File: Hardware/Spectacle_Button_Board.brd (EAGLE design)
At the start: 44.5 x 73.7 mm, 46 parts, among them J17 AUDIO-JACK3, J19 FTDI_DEVICE, J20 AUDIO-JACK3, U1 CY8C4146LQI-S422, U2 3.3V/150mA

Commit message: first draft routing
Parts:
- moved C5 40.0 mm to (20.6, 25.0), turned to 180 degrees
- moved R2 37.7 mm to (29.5, 25.0)
- moved C6 37.7 mm to (20.8, 26.8), turned to 180 degrees
- moved D3 36.7 mm to (22.1, 29.6)
- moved C4 33.7 mm to (27.4, 42.0), turned to 90 degrees
- moved C2 33.0 mm to (24.4, 42.0)
- moved D2 33.0 mm to (28.1, 50.2)
- moved D4 33.0 mm to (15.2, 48.3)
- moved D5 33.0 mm to (15.2, 52.1)
- moved D6 33.0 mm to (15.2, 44.5)
- moved D7 33.0 mm to (15.2, 36.8)
- moved D8 33.0 mm to (15.2, 40.6)
- moved D9 33.0 mm to (15.2, 33.0)
- moved J1 33.0 mm to (27.2, 57.0)
- moved J10 33.0 mm to (36.8, 68.6)
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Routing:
- net GND: track 37.4 -> 12.6 mm, vias 0 -> 2
- net N$3: track 10.2 -> 1.40 mm
- net VIN: track 51.7 -> 46.6 mm
- net N$5: track 8.66 -> 4.85 mm
- net 3.3V: track 79.1 -> 75.3 mm
- net SCL: track 44.3 -> 46.2 mm

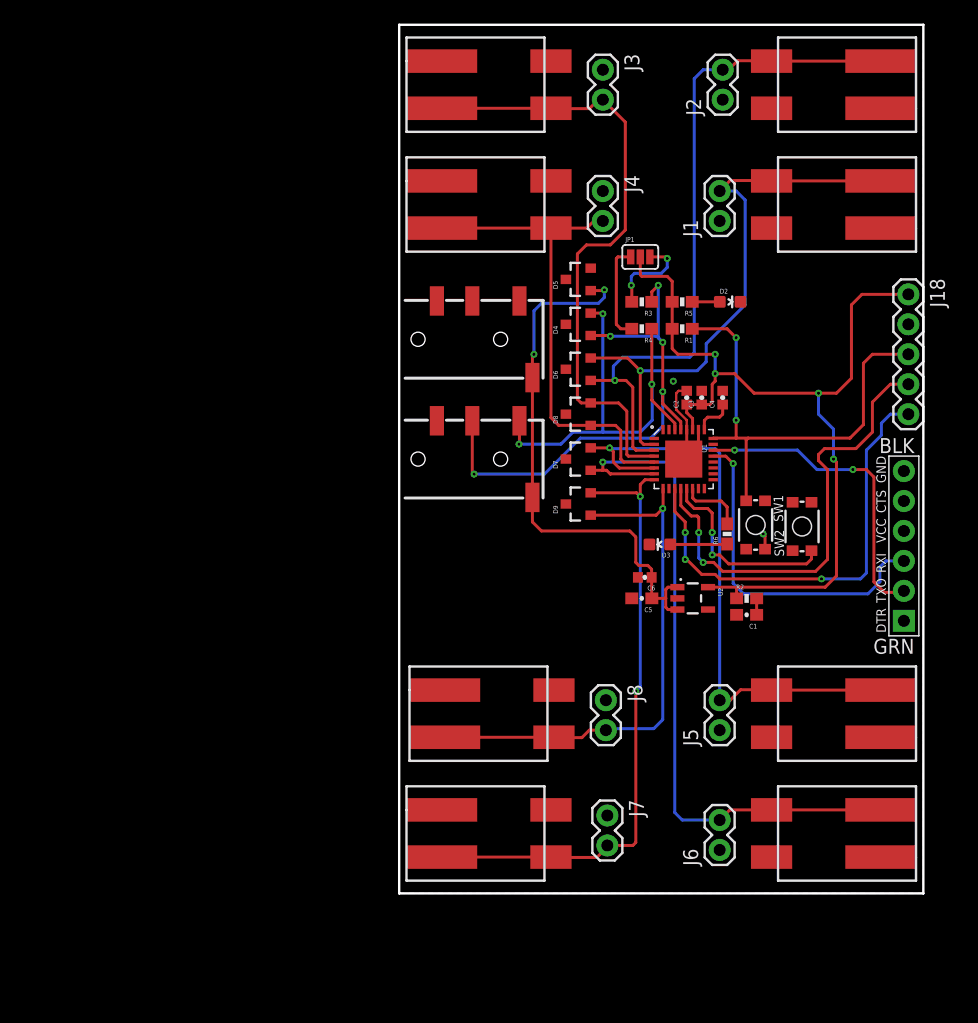
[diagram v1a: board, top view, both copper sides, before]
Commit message: added silk and dimensions
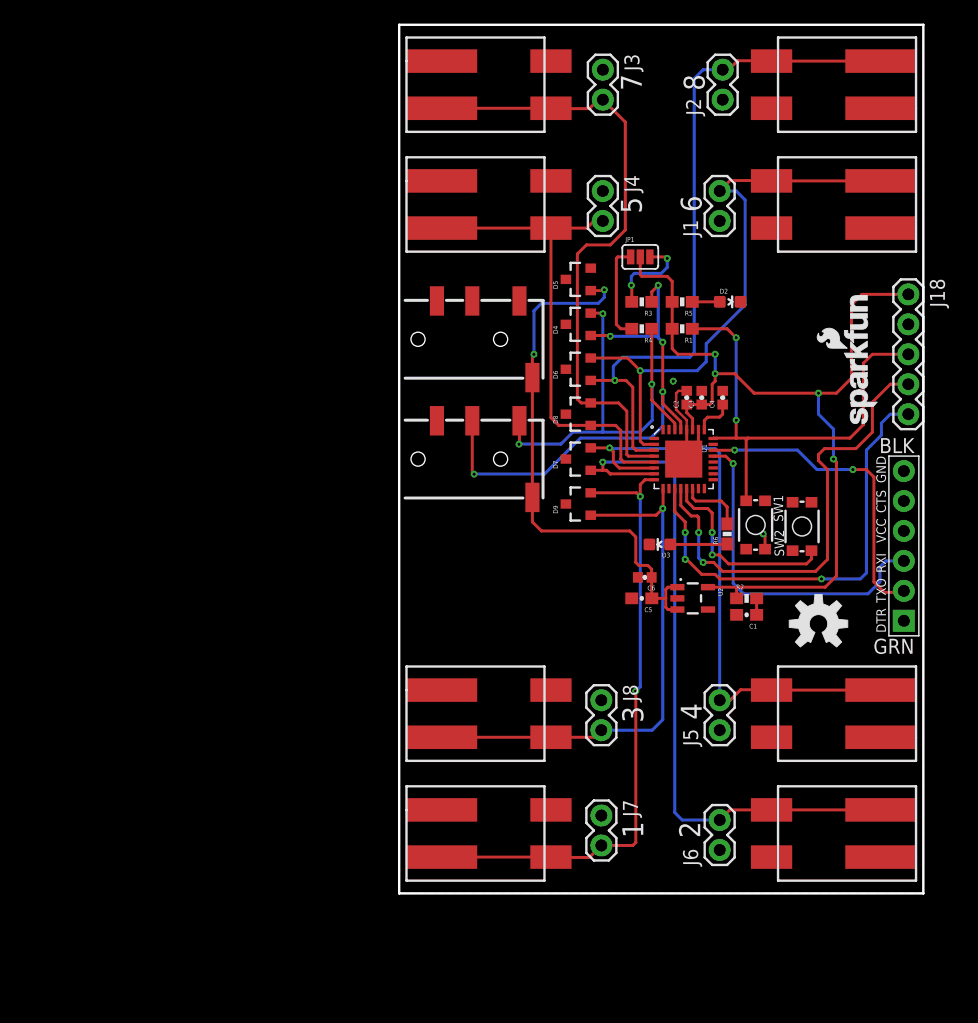
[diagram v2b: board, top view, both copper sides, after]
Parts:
- added LOGO1, LOGO4: OSHW-LOGOM, SparkFun-Aesthetics:OSHW-LOGO-M
- added LOGO2, LOGO3: SFE_LOGO_NAME_FLAME.1_INCH, SparkFun-Aesthetics:SFE_LOGO_NAME_FLAME_.1
- moved J7 0.51 mm to (17.1, 6.60)
- moved J8 0.38 mm to (17.1, 16.4)
- moved J16 0.25 mm to (7.62, 15.2)
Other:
- board text added: "1"
- board text added: "2"
- board text added: "3"
- board text added: "4"
- board text added: "5"
- board text added: "6"
- board text added: "7"
- board text added: "8"
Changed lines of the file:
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@@
 <wire x1="44.45" y1="0" x2="44.45" y2="73.66" width="0.2032" layer="20"/>
 <wire x1="0" y1="73.66" x2="44.45" y2="73.66" width="0.2032" layer="20"/>
+<dimension x1="0" y1="73.66" x2="44.45" y2="73.66" x3="22.225" y3="78.74" textsize="1.778" textratio="15" layer="20" unit="inch"/>
+<dimension x1="44.45" y1="73.66" x2="44.45" y2="0" x3="50.8" y3="36.83" textsize="1.778" textratio="15" layer="20" unit="inch"/>
+<text x="20.701" y="4.699" size="1.778" layer="21" font="vector" ratio="15" rot="R90">1</text>
+<text x="25.527" y="4.699" size="1.778" layer="21" font="vector" ratio="15" rot="R90">2</text>
+<text x="20.701" y="14.478" size="1.778" layer="21" font="vector" ratio="15" rot="R90">3</text>
+<text x="23.876" y="16.129" size="1.778" layer="21" font="vector" ratio="15" rot="R270">4</text>
+<text x="20.574" y="57.658" size="1.778" layer="21" font="vector" ratio="15" rot="R90">5</text>
+<text x="25.654" y="57.785" size="1.778" layer="21" font="vector" ratio="15" rot="R90">6</text>
+<text x="20.574" y="68.072" size="1.778" layer="21" font="vector" ratio="15" rot="R90">7</text>
+<text x="25.908" y="68.072" size="1.778" layer="21" font="vector" ratio="15" rot="R90">8</text>
 </plain>
 <attributes>
@@
 <element name="J5" library="SparkFun-Connectors" package="1X02" value="" x="27.178" y="13.843" rot="R90"/>
 <element name="J6" library="SparkFun-Connectors" package="1X02" value="" x="27.178" y="3.683" rot="R90"/>
-<element name="J7" library="SparkFun-Connectors" package="1X02" value="" x="17.653" y="6.604" rot="R270"/>
-<element name="J8" library="SparkFun-Connectors" package="1X02" value="" x="17.526" y="16.383" rot="R270"/>
+<element name="J7" library="SparkFun-Connectors" package="1X02" value="" x="17.145" y="6.604" rot="R270"/>
+<element name="J8" library="SparkFun-Connectors" package="1X02" value="" x="17.145" y="16.383" rot="R270"/>
 <element name="J9" library="SparkFun-Connectors" package="1X02_POKEHOME" value="" x="36.83" y="58.42" rot="R180">
 <attribute name="PROD_ID" value="CONN-#####" x="36.83" y="58.42" size="1.778" layer="27" font="vector" ratio="15" rot="R180" display="off"/>
@@
 <attribute name="PROD_ID" value="CONN-#####" x="7.62" y="5.08" size="1.778" layer="27" font="vector" ratio="15" display="off"/>
 </element>
-<element name="J16" library="SparkFun-Connectors" package="1X02_POKEHOME" value="" x="7.874" y="15.24">
-<attribute name="PROD_ID" value="CONN-#####" x="7.874" y="15.24" size="1.778" layer="27" font="vector" ratio="15" display="off"/>
+<element name="J16" library="SparkFun-Connectors" package="1X02_POKEHOME" value="" x="7.62" y="15.24">
+<attribute name="PROD_ID" value="CONN-#####" x="7.62" y="15.24" size="1.778" layer="27" font="vector" ratio="15" display="off"/>
 </element>
 <element name="R1" library="SparkFun-Resistors" package="0603-RES" value="10K" x="24.003" y="47.879" rot="R180">
@@
 </element>
 <element name="J20" library="SparkFun-Connectors" package="AUDIO-JACK-TRRS-SMD" value="AUDIO-JACK3" x="0" y="46.99"/>
+<element name="LOGO1" library="SparkFun-Aesthetics" package="OSHW-LOGO-M" value="OSHW-LOGOM" x="35.56" y="22.86"/>
+<element name="LOGO2" library="SparkFun-Aesthetics" package="SFE_LOGO_NAME_FLAME_.1" value="SFE_LOGO_NAME_FLAME.1_INCH" x="40.64" y="39.37" rot="R90"/>
+<element name="LOGO3" library="SparkFun-Aesthetics" package="SFE_LOGO_NAME_FLAME_.1" value="SFE_LOGO_NAME_FLAME.1_INCH" x="40.64" y="50.8" rot="MR270"/>
+<element name="LOGO4" library="SparkFun-Aesthetics" package="OSHW-LOGO-M" value="OSHW-LOGOM" x="40.64" y="5.08" rot="MR270"/>
 </elements>
 <signals>
@@
 <contactref element="D9" pad="1"/>
 <contactref element="J16" pad="P4"/>
-<wire x1="3.874" y1="13.24" x2="13.124" y2="13.24" width="0.254" layer="1"/>
-<wire x1="17.526" y1="13.843" x2="16.129" y2="13.843" width="0.254" layer="1"/>
-<wire x1="16.129" y1="13.843" x2="15.494" y2="13.208" width="0.254" layer="1"/>
-<wire x1="15.494" y1="13.208" x2="13.156" y2="13.208" width="0.254" layer="1"/>
-<wire x1="13.156" y1="13.208" x2="13.124" y2="13.24" width="0.254" layer="1"/>
+<wire x1="3.62" y1="13.24" x2="12.87" y2="13.24" width="0.254" layer="1"/>
 <wire x1="22.38" y1="34.33" x2="22.38" y2="32.667" width="0.254" layer="1"/>
 <wire x1="22.38" y1="32.667" x2="22.352" y2="32.639" width="0.254" layer="1"/>
 <via x="22.352" y="32.639" extent="1-16" drill="0.254"/>
 <wire x1="22.352" y1="32.639" x2="22.352" y2="14.732" width="0.254" layer="16"/>
-<wire x1="22.352" y1="14.732" x2="21.59" y2="13.97" width="0.254" layer="16"/>
-<wire x1="21.59" y1="13.97" x2="17.653" y2="13.97" width="0.254" layer="16"/>
-<wire x1="17.653" y1="13.97" x2="17.526" y2="13.843" width="0.254" layer="16"/>
+<wire x1="22.352" y1="14.732" x2="21.463" y2="13.843" width="0.254" layer="16"/>
 <wire x1="16.24" y1="32.07" x2="21.783" y2="32.07" width="0.254" layer="1"/>
 <wire x1="21.783" y1="32.07" x2="22.352" y2="32.639" width="0.254" layer="1"/>
+<wire x1="17.145" y1="13.843" x2="21.463" y2="13.843" width="0.254" layer="16"/>
+<wire x1="12.87" y1="13.24" x2="16.542" y2="13.24" width="0.254" layer="1"/>
+<wire x1="16.542" y1="13.24" x2="17.145" y2="13.843" width="0.254" layer="1"/>
 </signal>
 <signal name="IN_5">
@@
 <contactref element="D9" pad="2"/>
 <contactref element="J15" pad="P4"/>
-<wire x1="17.653" y1="4.064" x2="17.653" y2="3.937" width="0.254" layer="1"/>
-<wire x1="17.653" y1="3.937" x2="16.764" y2="3.048" width="0.254" layer="1"/>
-<wire x1="16.764" y1="3.048" x2="12.902" y2="3.048" width="0.254" layer="1"/>
 <wire x1="12.902" y1="3.048" x2="12.87" y2="3.08" width="0.254" layer="1"/>
 <wire x1="3.62" y1="3.08" x2="12.87" y2="3.08" width="0.254" layer="1"/>
-<wire x1="17.653" y1="4.064" x2="19.812" y2="4.064" width="0.254" layer="1"/>
 <wire x1="19.812" y1="4.064" x2="20.066" y2="4.318" width="0.254" layer="1"/>
 <wire x1="20.066" y1="4.318" x2="20.066" y2="17.145" width="0.254" layer="1"/>
@@
 <wire x1="16.24" y1="33.97" x2="20.132" y2="33.97" width="0.254" layer="1"/>
 <wire x1="20.132" y1="33.97" x2="20.447" y2="33.655" width="0.254" layer="1"/>
+<wire x1="19.812" y1="4.064" x2="17.145" y2="4.064" width="0.254" layer="1"/>
+<wire x1="12.902" y1="3.048" x2="16.129" y2="3.048" width="0.254" layer="1"/>
+<wire x1="16.129" y1="3.048" x2="17.145" y2="4.064" width="0.254" layer="1"/>
 </signal>
 <signal name="VCC">

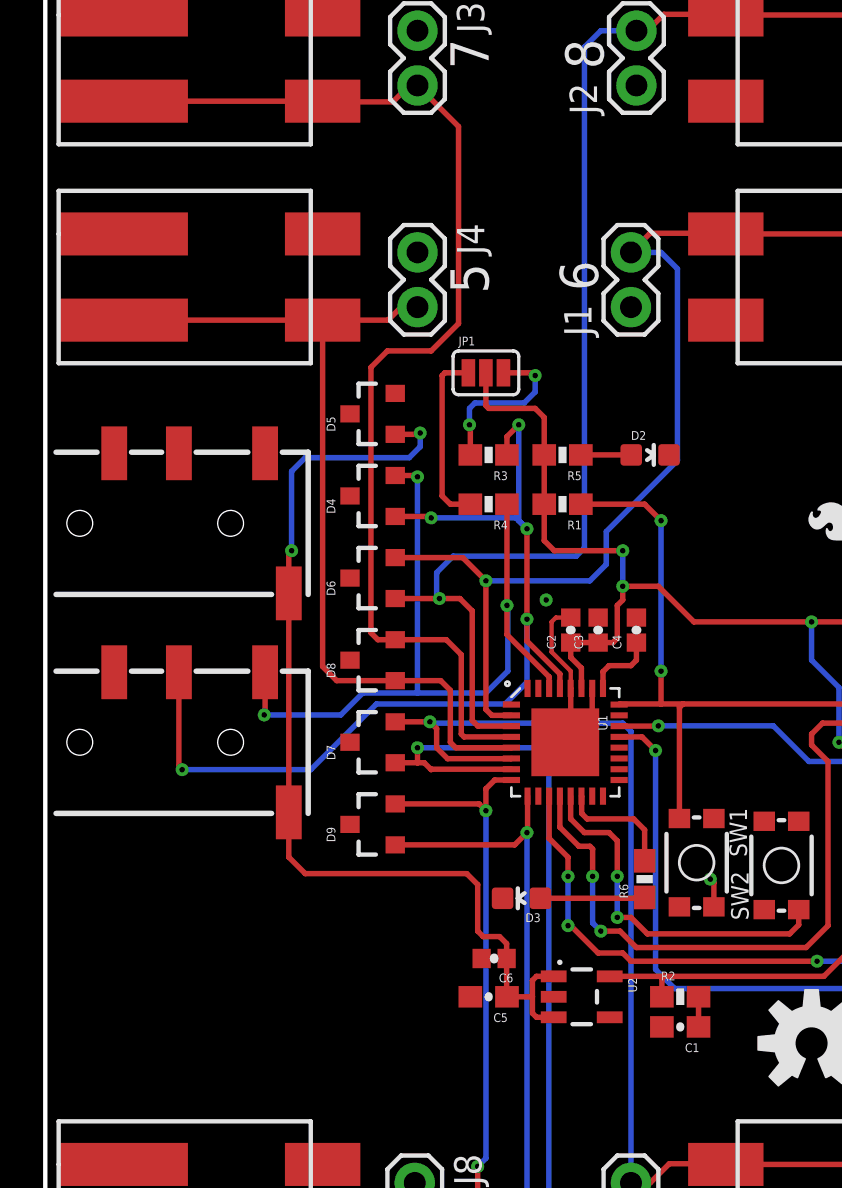
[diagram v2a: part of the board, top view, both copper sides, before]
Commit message: Added spectacle logos
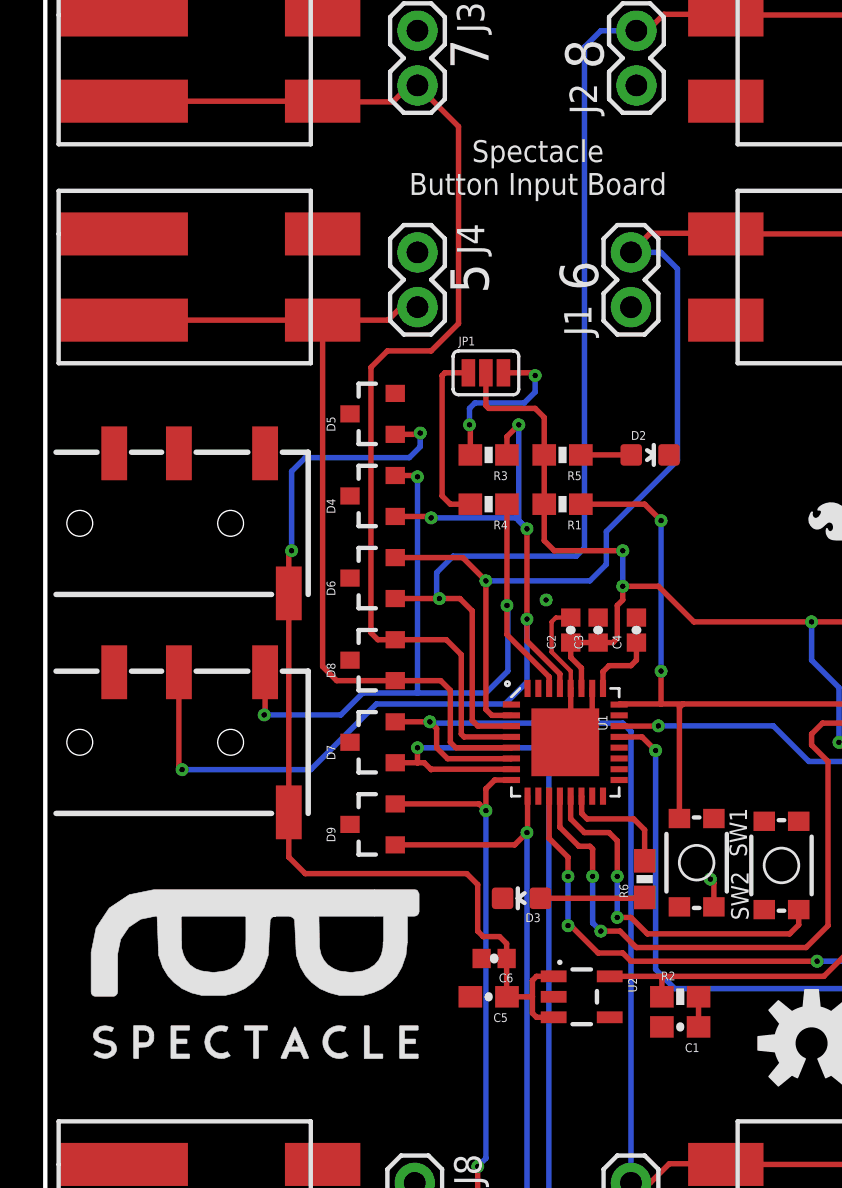
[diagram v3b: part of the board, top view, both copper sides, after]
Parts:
- removed LOGO3: SFE_LOGO_NAME_FLAME.1_INCH, SparkFun-Aesthetics:SFE_LOGO_NAME_FLAME_.1
- removed LOGO4: OSHW-LOGOM, SparkFun-Aesthetics:OSHW-LOGO-M
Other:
- board text added: "Spectacle Button Input Board"

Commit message: Final for review
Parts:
- added FD1, FD2: FIDUCIALUFIDUCIAL, SparkFun-Aesthetics:MICRO-FIDUCIAL
- moved FRAME1 93.4 mm to (-66.0, -16.5)
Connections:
- net SDA: now also J20.RING1, J20.TIP
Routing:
- net SDA: track 37.7 -> 58.9 mm, vias 3 -> 4
- net SCL: track 46.2 -> 43.4 mm
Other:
- board text added: "Mike Hord and Dia Campbell"
- board text added: "PWR"
- board text added: "RESET"
- board text added: "V01"

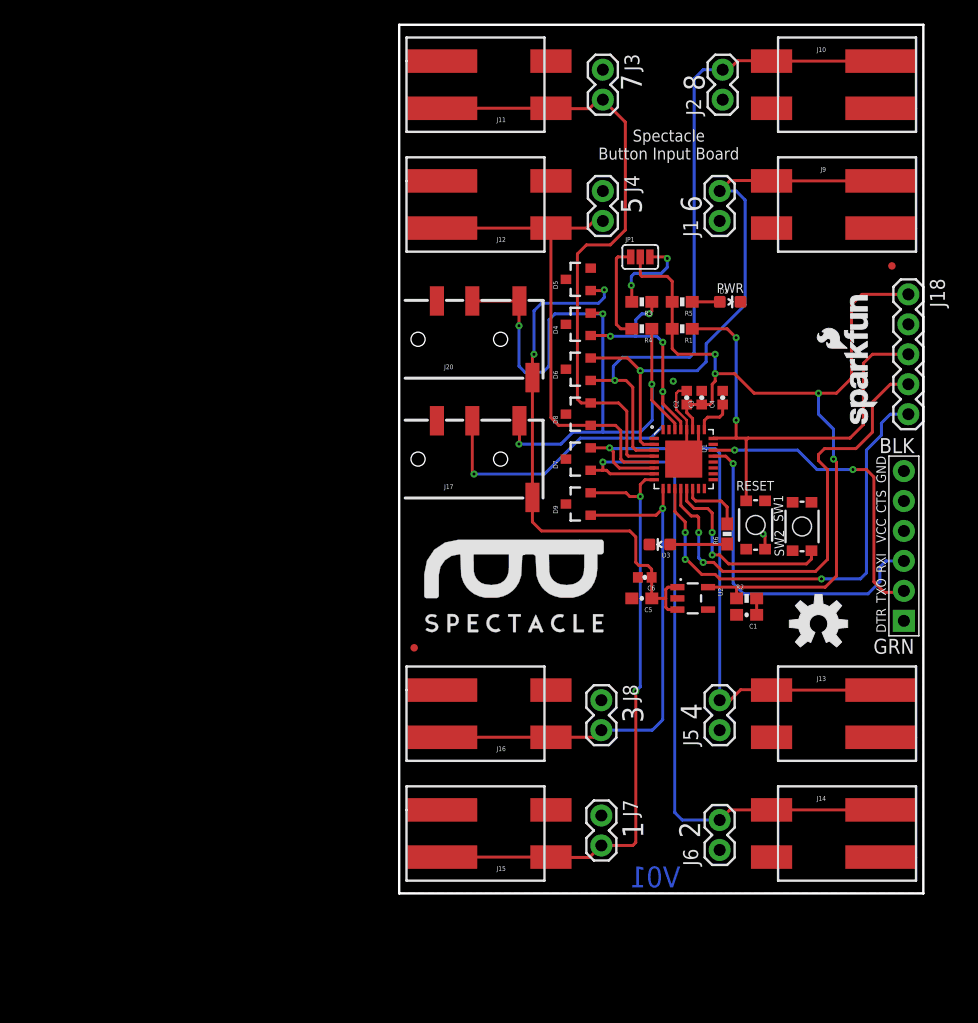
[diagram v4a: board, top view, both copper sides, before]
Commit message: added staking vias, straightened headers
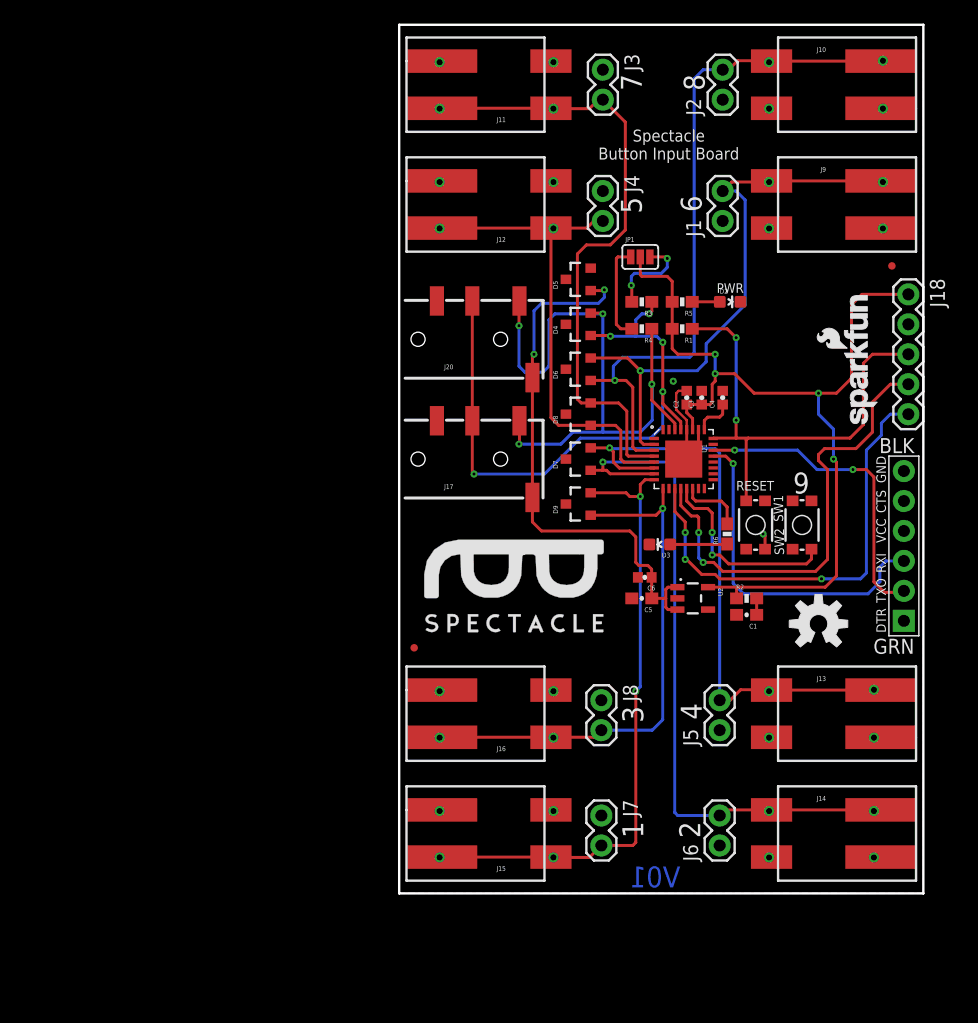
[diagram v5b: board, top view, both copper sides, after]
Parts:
- moved J6 0.38 mm to (27.2, 4.06)
- moved J1 0.25 mm to (27.4, 57.0)
- moved SW2 0.13 mm to (34.2, 31.2)
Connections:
- net SCL: now also J20.RING1
- net SDA: no longer J20.RING1
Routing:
- net SCL: track 43.4 -> 53.6 mm
- net SDA: track 58.9 -> 54.9 mm
- net IN_1: track 59.1 -> 62.5 mm, vias 1 -> 3
- net IN_7: track 45.3 -> 48.6 mm, vias 1 -> 3
- net IN_3: track 41.7 -> 45.0 mm, vias 0 -> 2
- net IN_0: track 49.4 -> 52.0 mm, vias 1 -> 3
- net IN_2: track 53.7 -> 55.4 mm, vias 0 -> 2
- net IN_4: track 51.1 -> 52.3 mm, vias 1 -> 3
- net IN_6: vias 2 -> 4
- net GND: vias 2 -> 18
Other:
- board text added: "9"

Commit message: Quick schematic changes, ready for QC review
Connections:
- net GND: now also J17.TIP, J20.TIP; no longer J17.RING2, J20.RING2
- net SCL: now also J17.RING2, J20.RING2; no longer J17.RING1, J20.RING1
- net SDA: now also J17.RING1, J20.RING1; no longer J17.TIP, J20.TIP
- net VIN: now also D5.2; no longer D5.1
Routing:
- net SDA: track 54.9 -> 63.4 mm, vias 4 -> 5
- net SCL: track 53.6 -> 56.3 mm
- net VIN: track 46.6 -> 49.0 mm
- net IN_6: track 53.2 -> 54.9 mm
